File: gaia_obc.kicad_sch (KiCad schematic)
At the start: 59 parts, among them J1 USB_C_Receptacle_USB2.0_16P, J2 Conn_02x10_Odd_Even, J3 Conn_02x10_Odd_Even, Q1 IRLML6244, SW1 SW_Push, SW2 SW_Push, U1 MCP23017_ML, U2 USBLC6-2P6, U3 ESP32-S3-PICO-1-N8R2

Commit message: obc v1.2-pre1
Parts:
- removed D1: LED_Small, LED_SMD:LED_0603_1608Metric, symbol Device:LED_Small
- removed R6: TBA, Resistor_SMD:R_0402_1005Metric, symbol Device:R_Small

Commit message: v1.2
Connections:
- net +BATT renamed PRI_HI
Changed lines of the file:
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@@
 	)
 	(symbol
+		(lib_id "power:PRI_HI")
+		(at 92.71 48.26 270)
+		(unit 1)
+		(exclude_from_sim no)
+		(in_bom yes)
+		(on_board yes)
+		(dnp no)
+		(fields_autoplaced yes)
+		(property "Reference" "#PWR030"
+			(at 88.9 48.26 0)
+			(effects
+				(font
+					(size 1.27 1.27)
+				)
+				(hide yes)
+			)
+		)
+		(property "Value" "PRI_HI"
+			(at 96.52 48.2599 90)
+			(effects
+				(font
+					(size 1.27 1.27)
+				)
+				(justify left)
+			)
+		)
+		(property "Footprint" ""
+			(at 92.71 48.26 0)
+			(effects
+				(font
+					(size 1.27 1.27)
+				)
+				(hide yes)
+			)
+		)
+		(property "Datasheet" ""
+			(at 92.71 48.26 0)
+			(effects
+				(font
+					(size 1.27 1.27)
+				)
+				(hide yes)
+			)
+		)
+		(property "Description" "Power symbol creates a global label with name \"PRI_HI\""
+			(at 92.71 48.26 0)
+			(effects
+				(font
+					(size 1.27 1.27)
+				)
+				(hide yes)
+			)
+		)
+		(pin "1"
+		)
+		(instances
+			(project "gaia_obc"
+				(path "/049f7784-e0f9-4d41-b308-330ac61e4408"
+					(reference "#PWR030")
+					(unit 1)
+				)
+			)
+		)
+	)
+	(symbol
 		(lib_id "power:GND")
 		(at 97.79 182.88 90)
@@
 	)
 	(symbol
-		(lib_id "power:+BATT")
-		(at 80.01 48.26 90)
-		(unit 1)
-		(exclude_from_sim no)
-		(in_bom yes)
-		(on_board yes)
-		(dnp no)
-		(fields_autoplaced yes)
-		(property "Reference" "#PWR024"
-			(at 83.82 48.26 0)
-			(effects
-				(font
-					(size 1.27 1.27)
-				)
-				(hide yes)
-			)
-		)
-		(property "Value" "+BATT"
-			(at 76.2 48.2599 90)
-			(effects
-				(font
-					(size 1.27 1.27)
-				)
-				(justify left)
-			)
-		)
-		(property "Footprint" ""
-			(at 80.01 48.26 0)
-			(effects
-				(font
-					(size 1.27 1.27)
-				)
-				(hide yes)
-			)
-		)
-		(property "Datasheet" ""
-			(at 80.01 48.26 0)
-			(effects
-				(font
-					(size 1.27 1.27)
-				)
-				(hide yes)
-			)
-		)
-		(property "Description" "Power symbol creates a global label with name \"+BATT\""
-			(at 80.01 48.26 0)
-			(effects
-				(font
-					(size 1.27 1.27)
-				)
-				(hide yes)
-			)
-		)
-		(pin "1"
-		)
-		(instances
-			(project "gaia_obc"
-				(path "/049f7784-e0f9-4d41-b308-330ac61e4408"
-					(reference "#PWR024")
-					(unit 1)
-				)
-			)
-		)
-	)
-	(symbol
 		(lib_id "power:GND")
 		(at 134.62 34.29 270)
@@
 	)
 	(symbol
-		(lib_id "power:+BATT")
-		(at 92.71 48.26 270)
-		(unit 1)
-		(exclude_from_sim no)
-		(in_bom yes)
-		(on_board yes)
-		(dnp no)
-		(fields_autoplaced yes)
-		(property "Reference" "#PWR030"
-			(at 88.9 48.26 0)
-			(effects
-				(font
-					(size 1.27 1.27)
-				)
-				(hide yes)
-			)
-		)
-		(property "Value" "+BATT"
-			(at 96.52 48.2599 90)
-			(effects
-				(font
-					(size 1.27 1.27)
-				)
-				(justify left)
-			)
-		)
-		(property "Footprint" ""
-			(at 92.71 48.26 0)
-			(effects
-				(font
-					(size 1.27 1.27)
-				)
-				(hide yes)
-			)
-		)
-		(property "Datasheet" ""
-			(at 92.71 48.26 0)
-			(effects
-				(font
-					(size 1.27 1.27)
-				)
-				(hide yes)
-			)
-		)
-		(property "Description" "Power symbol creates a global label with name \"+BATT\""
-			(at 92.71 48.26 0)
-			(effects
-				(font
-					(size 1.27 1.27)
-				)
-				(hide yes)
-			)
-		)
-		(pin "1"
-		)
-		(instances
-			(project "gaia_obc"
-				(path "/049f7784-e0f9-4d41-b308-330ac61e4408"
-					(reference "#PWR030")
-					(unit 1)
-				)
-			)
-		)
-	)
-	(symbol
 		(lib_id "Device:R_Small")
 		(at 223.52 48.26 0)
@@
 					(unit 1)
 				)
+			)
+		)
+	)
+	(symbol
+		(lib_id "power:PRI_HI")
+		(at 80.01 48.26 90)
+		(unit 1)
+		(exclude_from_sim no)
+		(in_bom yes)
+		(on_board yes)
+		(dnp no)
+		(fields_autoplaced yes)
+		(property "Reference" "#PWR024"
+			(at 83.82 48.26 0)
+			(effects
+				(font
+					(size 1.27 1.27)
+				)
+				(hide yes)
+			)
+		)
+		(property "Value" "PRI_HI"
+			(at 76.2 48.2599 90)
+			(effects
+				(font
+					(size 1.27 1.27)
+				)
+				(justify left)
+			)
+		)
+		(property "Footprint" ""
+			(at 80.01 48.26 0)
+			(effects
+				(font
+					(size 1.27 1.27)
+				)
+				(hide yes)
+			)
+		)
+		(property "Datasheet" ""
+			(at 80.01 48.26 0)
+			(effects
+				(font
+					(size 1.27 1.27)
+				)
+				(hide yes)
+			)
+		)
+		(property "Description" "Power symbol creates a global label with name \"PRI_HI\""
+			(at 80.01 48.26 0)
+			(effects
+				(font
+					(size 1.27 1.27)
+				)
+				(hide yes)
+			)
+		)
+		(pin "1"
+		)
+		(instances
+			(project ""
+				(path "/049f7784-e0f9-4d41-b308-330ac61e4408"
+					(reference "#PWR024")
+					(unit 1)
+				)

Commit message: v1.3
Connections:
- net GND: now also J2.10 (Pin_10), J2.8 (Pin_8)
- net SPI_0_MISO: no longer J2.6 (Pin_6)
- net SPI_0_MOSI: no longer J2.8 (Pin_8)
- net SPI_0_SCLK: no longer J2.10 (Pin_10)
- new net VBACKUP: J2.6 (Pin_6)
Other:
- added sheet Battery Management System (bms.kicad_sch)

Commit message: neptune 1.3 production
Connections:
- net +3.3V: now also J2.8 (Pin_8)
- net GND: no longer J2.8 (Pin_8)
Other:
- title: GAIA On-Board Computer -> Neptune On-Board Computer
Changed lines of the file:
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@@
 	(paper "A4")
 	(title_block
-		(title "GAIA On-Board Computer")
-		(date "2025-12-01")
-		(rev "1.2")
+		(title "Neptune On-Board Computer")
+		(date "2025-12-12")
+		(rev "1.3")
 	)
 	(polyline
@@
 			(width 0.5)
 			(type solid)
+			(color 0 0 0 1)
 		)
 		(fill
 			(type color)
-			(color 0 0 0 0)
+			(color 0 0 0 1)
 		)
 	)
@@
 			(width 0.5)
 			(type solid)
+			(color 0 0 0 1)
 		)
 		(fill
 			(type color)
-			(color 0 0 0 0)
+			(color 0 0 0 1)
 		)
 	)
@@
 			(width 0.5)
 			(type solid)
+			(color 0 0 0 1)
 		)
 		(fill
 			(type color)
-			(color 0 0 0 0)
+			(color 0 0 0 1)
 		)
 	)
@@
 			(width 0.5)
 			(type solid)
+			(color 0 0 0 1)
 		)
 		(fill
 			(type color)
-			(color 0 0 0 0)
+			(color 0 0 0 1)
+		)
+	)
+	(rectangle
+		(start 109.22 154.94)
+		(end 175.26 196.85)
+		(stroke
+			(width 0)
+			(type default)
+		)
+		(fill
+			(type none)
 		)
 	)
@@
 			(width 0.5)
 			(type solid)
+			(color 0 0 0 1)
 		)
 		(fill
 			(type color)
-			(color 0 0 0 0)
+			(color 0 0 0 1)
 		)
 	)
@@
 			(width 0.5)
 			(type solid)
+			(color 0 0 0 1)
 		)
 		(fill
 			(type color)
-			(color 0 0 0 0)
+			(color 0 0 0 1)
 		)
 	)
@@
 			(width 0.5)
 			(type solid)
+			(color 0 0 0 1)
 		)
 		(fill
 			(type color)
-			(color 0 0 0 0)
+			(color 0 0 0 1)
 		)
 	)
 	(rectangle
 		(start 109.22 118.11)
-		(end 175.26 196.85)
+		(end 218.44 154.94)
 		(stroke
 			(width 0)
@@
 			(width 0.5)
 			(type solid)
+			(color 0 0 0 1)
 		)
 		(fill
 			(type color)
-			(color 0 0 0 0)
+			(color 0 0 0 1)
 		)
 	)
@@
 			(width 0.5)
 			(type solid)
+			(color 0 0 0 1)
 		)
 		(fill
 			(type color)
-			(color 0 0 0 0)
+			(color 0 0 0 1)
 		)
 	)
@@
 			(width 0.5)
 			(type solid)
+			(color 0 0 0 1)
 		)
 		(fill
 			(type color)
-			(color 0 0 0 0)
+			(color 0 0 0 1)
 		)
 	)
@@
 			(width 0.5)
 			(type solid)
+			(color 0 0 0 1)
 		)
 		(fill
 			(type color)
-			(color 0 0 0 0)
+			(color 0 0 0 1)
 		)
 	)
@@
 			(width 0.5)
 			(type solid)
+			(color 0 0 0 1)
 		)
 		(fill
 			(type color)
-			(color 0 0 0 0)
+			(color 0 0 0 1)
 		)
 	)
@@
 			(width 0.5)
 			(type solid)
+			(color 0 0 0 1)
 		)
 		(fill
 			(type color)
-			(color 0 0 0 0)
+			(color 0 0 0 1)
 		)
 	)
@@
 	(polyline
 		(pts
-			(xy 109.22 156.21) (xy 175.26 156.21)
+			(xy 175.26 118.11) (xy 175.26 154.94)
 		)
 		(stroke
@@
 	(symbol
 		(lib_id "power:GND")
-		(at 50.8 35.56 90)
-		(unit 1)
-		(exclude_from_sim no)
-		(in_bom yes)
-		(on_board yes)
-		(dnp no)
-		(fields_autoplaced yes)
-		(property "Reference" "#PWR0113"
-			(at 57.15 35.56 0)
-			(effects
-				(font
-					(size 1.27 1.27)
-				)
-				(hide yes)
-			)
-		)
-		(property "Value" "GND"
-			(at 54.61 35.5599 90)
-			(effects
-				(font
-					(size 1.27 1.27)
-				)
-				(justify right)
-			)
-		)
-		(property "Footprint" ""
-			(at 50.8 35.56 0)
-			(effects
-				(font
-					(size 1.27 1.27)
-				)
-				(hide yes)
-			)
-		)
-		(property "Datasheet" ""
-			(at 50.8 35.56 0)
-			(effects
-				(font
-					(size 1.27 1.27)
-				)
-				(hide yes)
-			)
-		)
-		(property "Description" "Power symbol creates a global label with name \"GND\" , ground"
-			(at 50.8 35.56 0)
-			(effects
-				(font
-					(size 1.27 1.27)
-				)
-				(hide yes)
-			)
-		)
-		(pin "1"
-		)
-		(instances
-			(project "gaia_obc"
-				(path "/049f7784-e0f9-4d41-b308-330ac61e4408"
-					(reference "#PWR0113")
-					(unit 1)
-				)
-			)
-		)
-	)
-	(symbol
-		(lib_id "power:GND")
 		(at 274.32 39.37 0)
 		(unit 1)
@@
 	)
 	(symbol
+		(lib_id "power:+3.3V")
+		(at 50.8 35.56 270)
+		(unit 1)
+		(exclude_from_sim no)
+		(in_bom yes)
+		(on_board yes)
+		(dnp no)
+		(property "Reference" "#PWR0113"
+			(at 46.99 35.56 0)
+			(effects
+				(font
+					(size 1.27 1.27)
+				)
+				(hide yes)
+			)
+		)
+		(property "Value" "+3.3V"
+			(at 53.848 35.56 90)
+			(effects
+				(font
+					(size 1.27 1.27)
+				)
+				(justify left)
+			)
+		)
+		(property "Footprint" ""
+			(at 50.8 35.56 0)
+			(effects
+				(font
+					(size 1.27 1.27)
+				)
+				(hide yes)
+			)
+		)
+		(property "Datasheet" ""
+			(at 50.8 35.56 0)
+			(effects
+				(font
+					(size 1.27 1.27)
+				)
+				(hide yes)
+			)
+		)
+		(property "Description" "Power symbol creates a global label with name \"+3.3V\""
+			(at 50.8 35.56 0)
+			(effects
+				(font
+					(size 1.27 1.27)
+				)
+				(hide yes)
+			)
+		)
+		(pin "1"
+		)
+		(instances
+			(project "gaia_obc"
+				(path "/049f7784-e0f9-4d41-b308-330ac61e4408"
+					(reference "#PWR0113")
+					(unit 1)
+				)
+			)
+		)
+	)
+	(symbol
 		(lib_id "power:GND")
 		(at 120.65 45.72 270)
@@
 	)
 	(sheet
-		(at 195.58 135.89)
-		(size 31.75 16.51)
+		(at 184.15 130.81)
+		(size 22.86 11.43)
 		(exclude_from_sim no)
 		(in_bom yes)
@@
 		)
 		(property "Sheetname" "Battery Management System"
-			(at 195.58 135.1784 0)
+			(at 184.15 130.0984 0)
 			(effects
 				(font
@@
 		)
 		(property "Sheetfile" "bms.kicad_sch"
-			(at 195.58 152.9846 0)
+			(at 184.15 142.8246 0)
 			(effects
 				(font

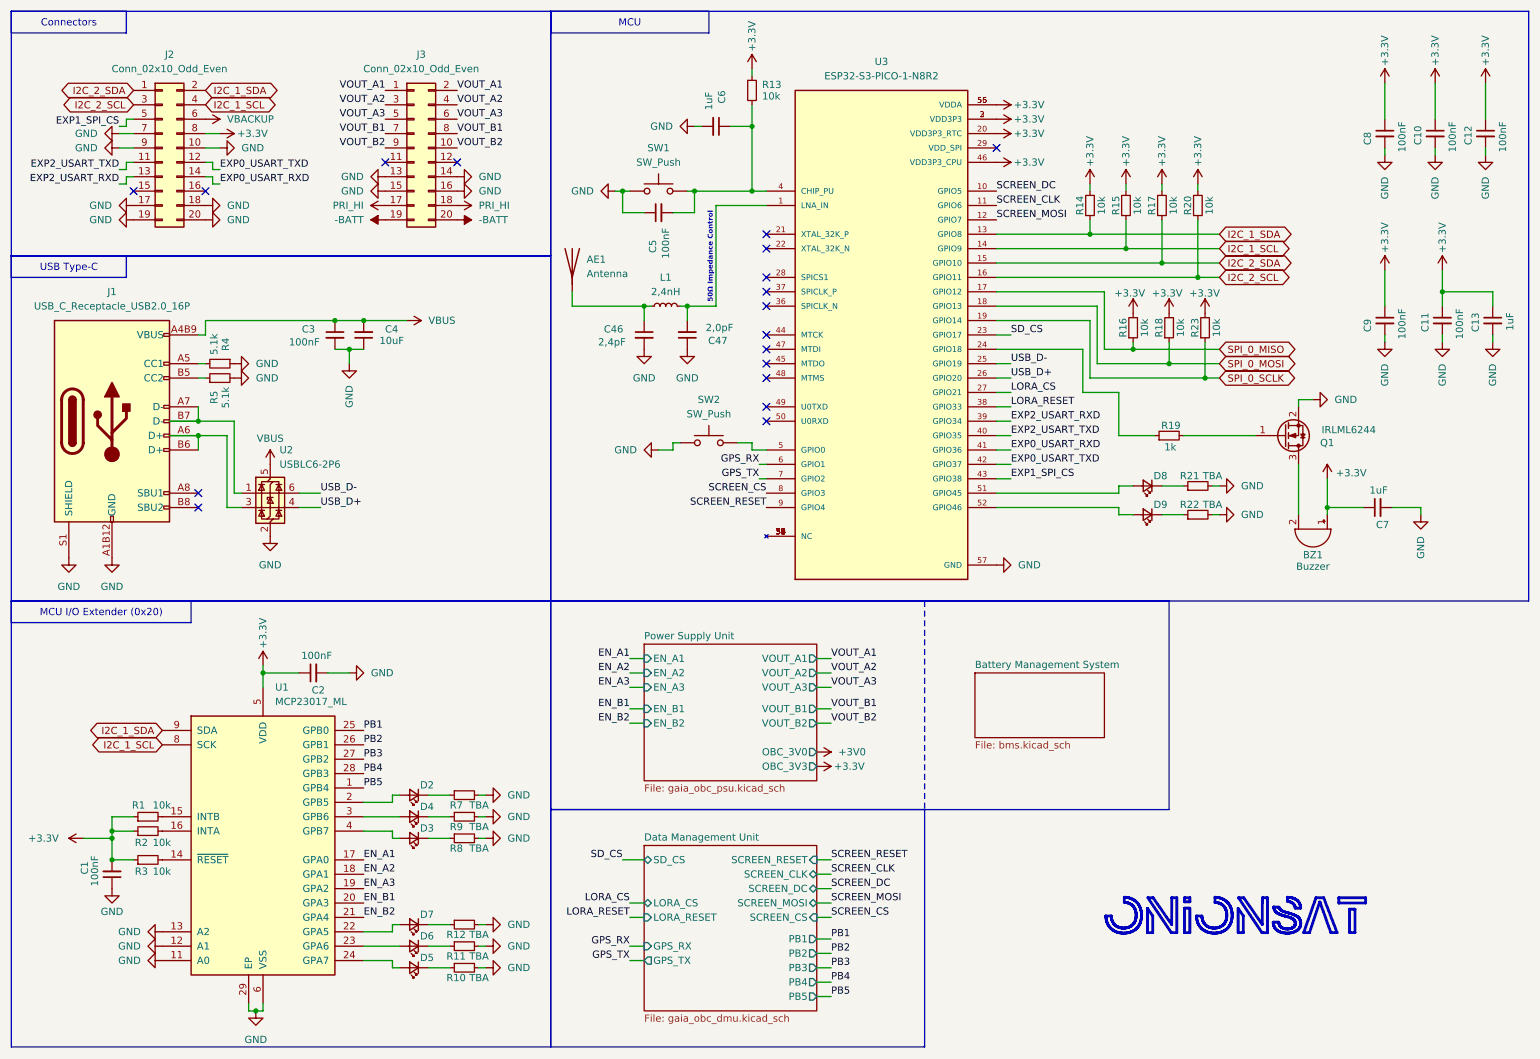
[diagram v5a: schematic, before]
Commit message: v1.4 - adding interrupt for lora
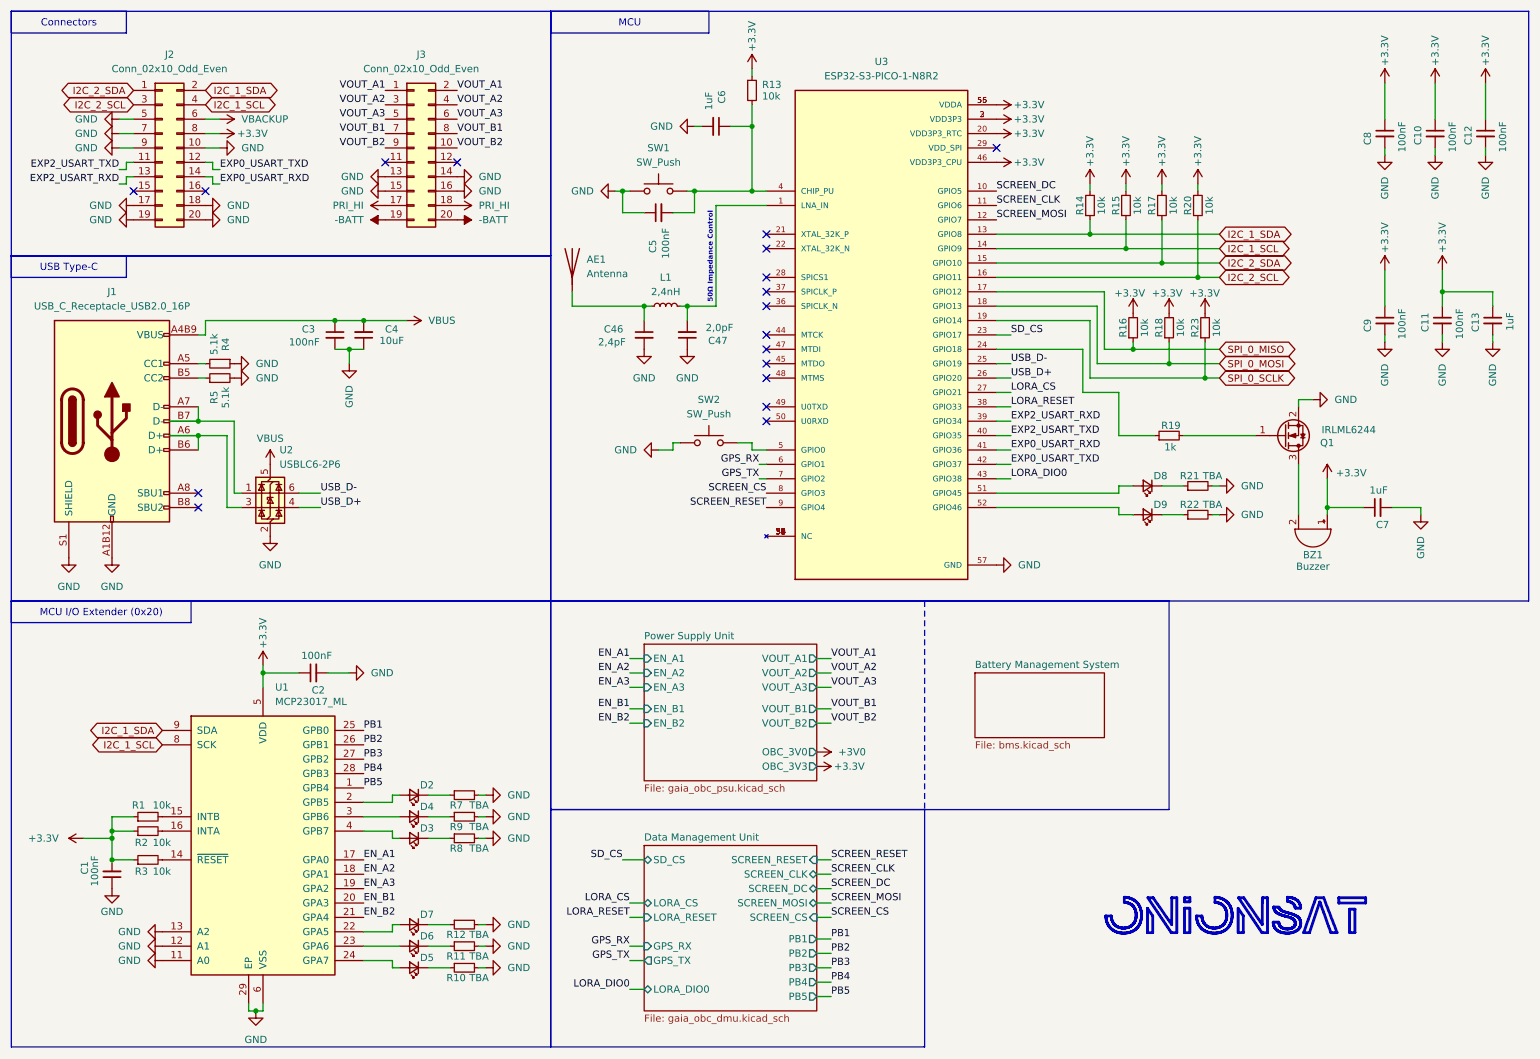
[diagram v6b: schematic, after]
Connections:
- net GND: now also J2.5 (Pin_5)
- net EXP1_SPI_CS renamed LORA_DIO0
- net LORA_DIO0: no longer J2.5 (Pin_5)
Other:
- sheet Data Management Unit ports: added LORA_DIO0; removed none
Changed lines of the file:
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@@
 	(title_block
 		(title "Neptune On-Board Computer")
-		(date "2025-12-12")
-		(rev "1.3")
+		(date "2025-12-28")
+		(rev "1.4")
 	)
 	(polyline
@@
 	(wire
 		(pts
-			(xy 34.29 34.29) (xy 34.29 33.02)
+			(xy 50.8 33.02) (xy 48.26 33.02)
 		)
 		(stroke
@@
 	(wire
 		(pts
-			(xy 33.02 34.29) (xy 34.29 34.29)
-		)
-		(stroke
-			(width 0)
-			(type default)
-		)
-	)
-	(wire
-		(pts
 			(xy 82.55 175.26) (xy 81.28 175.26)
 		)
@@
 	(wire
 		(pts
-			(xy 34.29 33.02) (xy 35.56 33.02)
-		)
-		(stroke
-			(width 0)
-			(type default)
-		)
-	)
-	(wire
-		(pts
 			(xy 52.07 88.9) (xy 46.99 88.9)
 		)
@@
 	(wire
 		(pts
+			(xy 33.02 33.02) (xy 35.56 33.02)
+		)
+		(stroke
+			(width 0)
+			(type default)
+		)
+	)
+	(wire
+		(pts
 			(xy 265.43 26.67) (xy 265.43 33.02)
 		)
@@
 	(wire
 		(pts
+			(xy 123.19 186.69) (xy 125.73 186.69)
+		)
+		(stroke
+			(width 0)
+			(type default)
+		)
+	)
+	(wire
+		(pts
 			(xy 187.96 58.42) (xy 217.17 58.42)
 		)
@@
 		)
 	)
-	(label "EXP1_SPI_CS"
-		(at 33.02 34.29 180)
-		(effects
-			(font
-				(size 1.27 1.27)
-			)
-			(justify right bottom)
-		)
-	)
 	(label "SCREEN_DC"
 		(at 187.96 45.72 0)
@@
 		)
 	)
+	(label "LORA_DIO0"
+		(at 123.19 186.69 180)
+		(effects
+			(font
+				(size 1.27 1.27)
+			)
+			(justify right bottom)
+		)
+	)
 	(label "EXP2_USART_TXD"
 		(at 33.02 41.91 180)
@@
 		)
 	)
-	(label "EXP1_SPI_CS"
+	(label "LORA_DIO0"
 		(at 190.5 96.52 0)
 		(effects
@@
 	)
 	(symbol
+		(lib_id "power:GND")
+		(at 33.02 33.02 270)
+		(unit 1)
+		(exclude_from_sim no)
+		(in_bom yes)
+		(on_board yes)
+		(dnp no)
+		(fields_autoplaced yes)
+		(property "Reference" "#PWR0200"
+			(at 26.67 33.02 0)
+			(effects
+				(font
+					(size 1.27 1.27)
+				)
+				(hide yes)
+			)
+		)
+		(property "Value" "GND"
+			(at 29.21 33.0199 90)
+			(effects
+				(font
+					(size 1.27 1.27)
+				)
+				(justify right)
+			)
+		)
+		(property "Footprint" ""
+			(at 33.02 33.02 0)
+			(effects
+				(font
+					(size 1.27 1.27)
+				)
+				(hide yes)
+			)
+		)
+		(property "Datasheet" ""
+			(at 33.02 33.02 0)
+			(effects
+				(font
+					(size 1.27 1.27)
+				)
+				(hide yes)
+			)
+		)
+		(property "Description" "Power symbol creates a global label with name \"GND\" , ground"
+			(at 33.02 33.02 0)
+			(effects
+				(font
+					(size 1.27 1.27)
+				)
+				(hide yes)
+			)
+		)
+		(pin "1"
+		)
+		(instances
+			(project "gaia_obc"
+				(path "/049f7784-e0f9-4d41-b308-330ac61e4408"
+					(reference "#PWR0200")
+					(unit 1)
+				)
+			)
+		)
+	)
+	(symbol
 		(lib_id "Interface_Expansion:MCP23017_ML")
 		(at 58.42 161.29 0)
@@
 	(symbol
 		(lib_id "power:VDC")
-		(at 48.26 33.02 270)
+		(at 50.8 33.02 270)
 		(unit 1)
 		(exclude_from_sim no)
@@
 		(fields_autoplaced yes)
 		(property "Reference" "#PWR0191"
-			(at 44.45 33.02 0)
+			(at 46.99 33.02 0)
 			(effects
 				(font
@@
 		)
 		(property "Value" "VBACKUP"
-			(at 52.07 33.0199 90)
+			(at 54.61 33.0199 90)
 			(effects
 				(font
@@
 		)
 		(property "Footprint" ""
-			(at 48.26 33.02 0)
+			(at 50.8 33.02 0)
 			(effects
 				(font
@@
 		)
 		(property "Datasheet" ""
-			(at 48.26 33.02 0)
+			(at 50.8 33.02 0)
 			(effects
 				(font
@@
 		)
 		(property "Description" "Power symbol creates a global label with name \"VDC\""
-			(at 48.26 33.02 0)
+			(at 50.8 33.02 0)
 			(effects
 				(font
@@
 			)
 		)
+		(pin "LORA_DIO0" bidirectional
+			(at 125.73 186.69 180)
+			(effects
+				(font
+					(size 1.27 1.27)
+				)
+				(justify left)
+			)
+		)
